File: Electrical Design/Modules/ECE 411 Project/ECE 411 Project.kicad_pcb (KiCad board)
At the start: 2 copper layers, 87.8 x 99.9 mm, 141 parts, among them J1 5mm 9V Barrel, J2 BOOST, J3 Pheonix Connector, J4 1/8in Jack, J5 1x2 header, J6 1x2header, J7 1x2header, M4 MountingHole_4.3mm_M4_Pad_Top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, Q2 2N3904, Q3 2N3904, Q4 2N3904, Q5 PNP, Q6 PNP, SW1 SW_Push, SW10 SW_SPDT, SW2 SW_Push, SW3 SW_Push, SW4 SW_Push, SW5 SW_Push, SW6 SW_Push, SW7 SW_Push, SW9 SW_SPDT, U1 HT7333, U2 LT1054, U3 MN3207, U4 NE555D, U5 LTV-827, U9 TPA3136D2PWPR

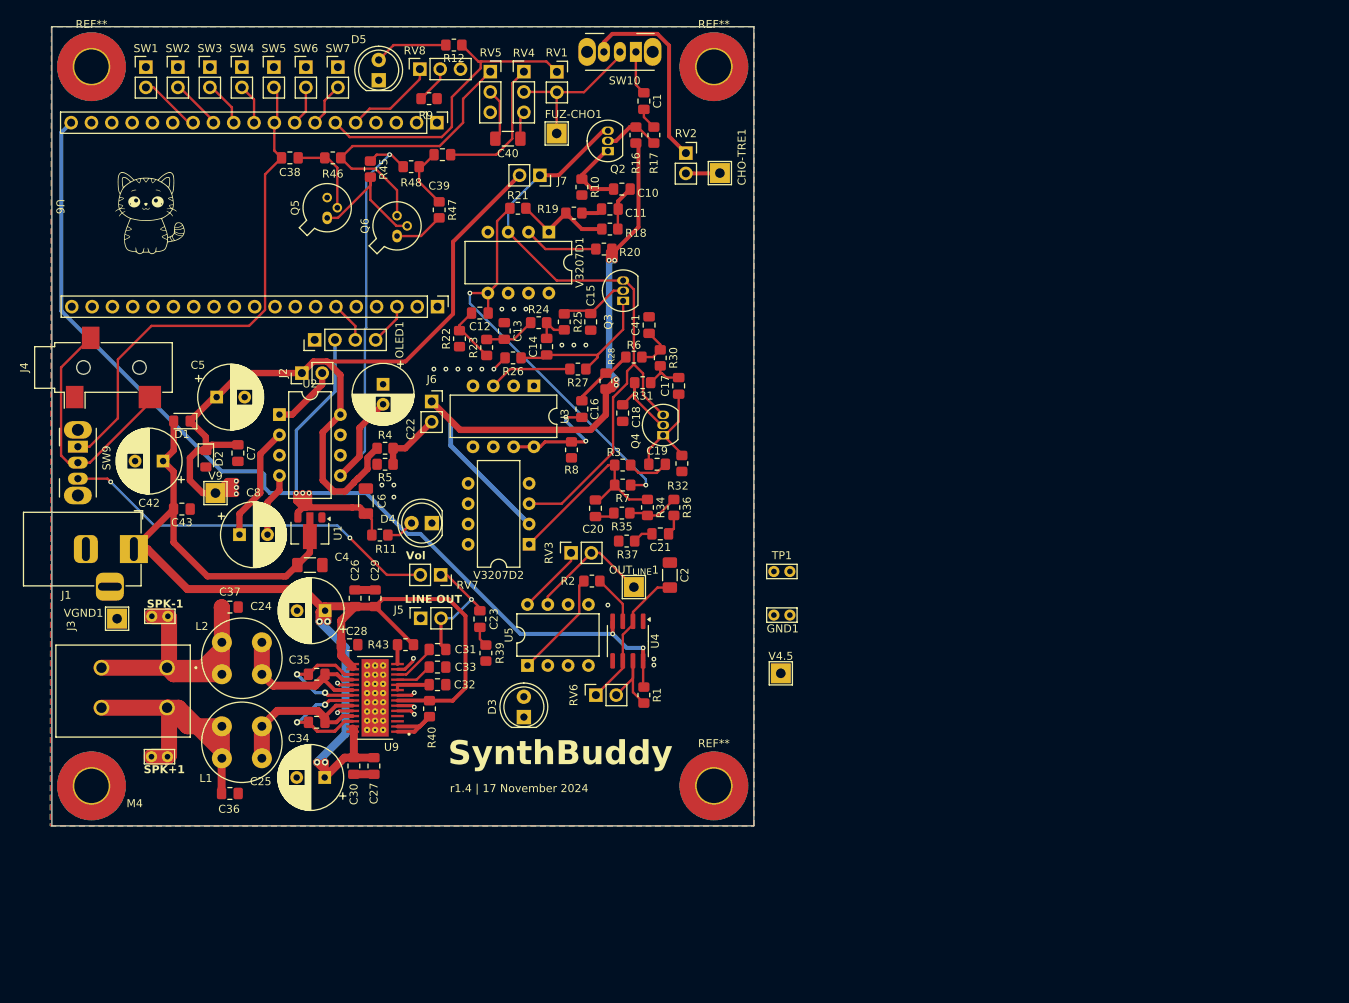
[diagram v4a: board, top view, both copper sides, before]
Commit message: add testpoints
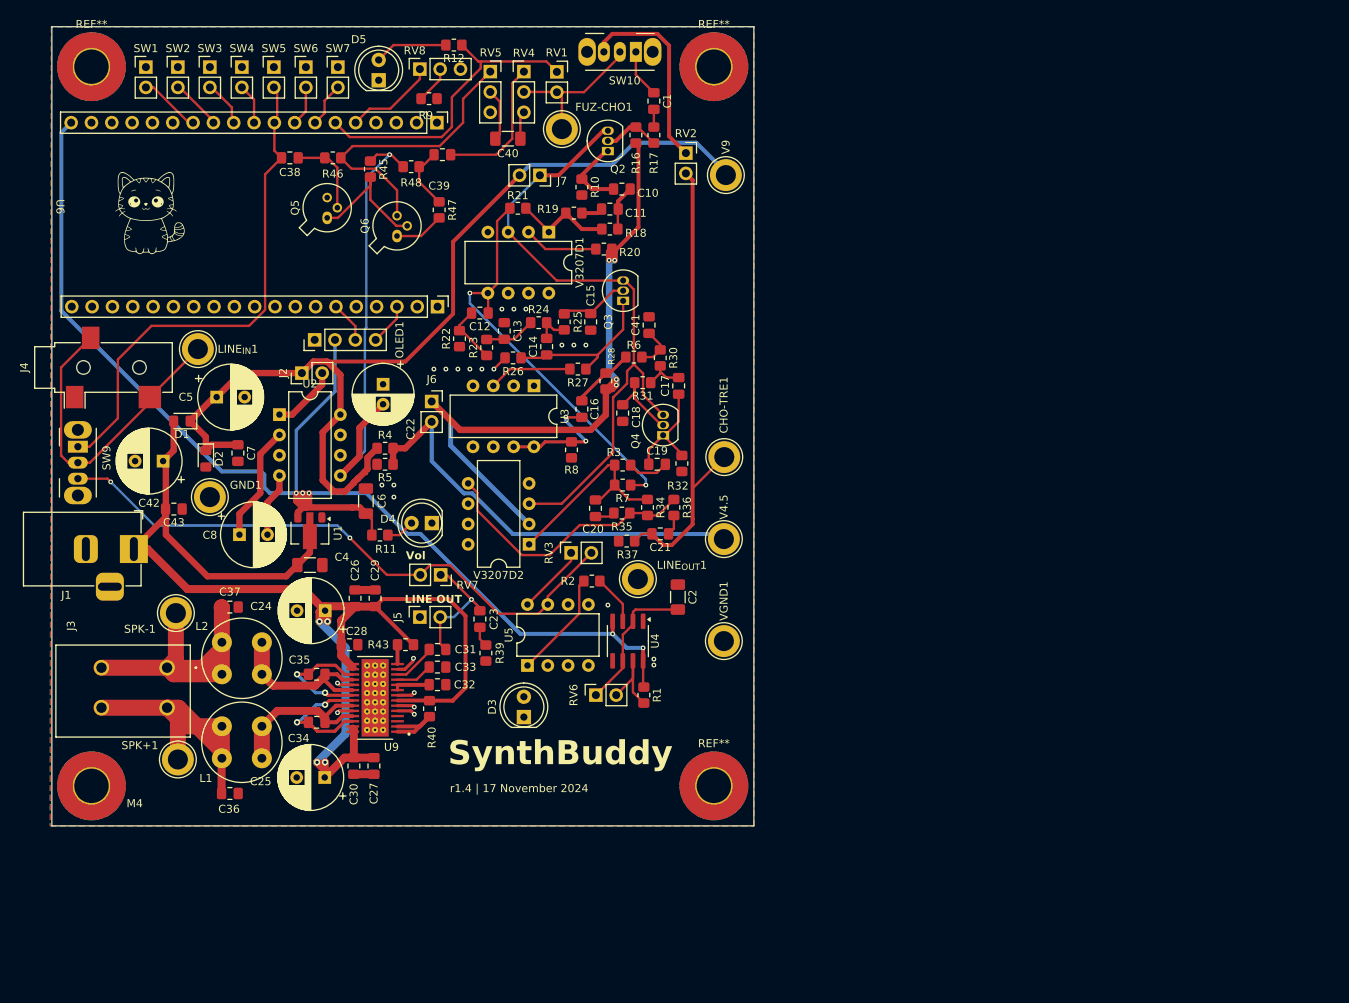
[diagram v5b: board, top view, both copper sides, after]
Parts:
- removed OUT_{LINE}1: TestPoint, TestPoint:TestPoint_THTPad_2.5x2.5mm_Drill1.2mm
- removed TP1: Line In, TestPoint:TestPoint_Bridge_Pitch2.0mm_Drill0.7mm
- added LINE_{IN}1: Line In, TestPoint:TestPoint_Loop_D3.80mm_Drill2.5mm, F.Cu at (50.0, 64.0)
- added LINE_{OUT}1: TestPoint, TestPoint:TestPoint_Loop_D3.80mm_Drill2.5mm, F.Cu at (105.0, 92.8)
- CHO-TRE1, FUZ-CHO1, V4.5, V9, VGND1: footprint TestPoint:TestPoint_THTPad_2.5x2.5mm_Drill1.2mm -> TestPoint:TestPoint_Loop_D3.80mm_Drill2.5mm
- GND1, SPK+1, SPK-1: footprint TestPoint:TestPoint_Bridge_Pitch2.0mm_Drill0.7mm -> TestPoint:TestPoint_Loop_D3.80mm_Drill2.5mm
- moved VGND1 75.9 mm to (115.8, 100.5)
- moved V9 75.2 mm to (116.0, 42.2), turned to 90 degrees
- moved GND1 72.0 mm to (51.5, 82.5)
- moved CHO-TRE1 35.5 mm to (115.8, 77.5)
- moved V4.5 18.2 mm to (115.8, 87.8), turned to 90 degrees
- moved SPK+1 3.32 mm to (47.5, 115.3)
- moved SPK-1 3.03 mm to (47.2, 97.0)
- moved C2 2.93 mm to (110.0, 95.0)
- moved C1 1.25 mm to (107.0, 33.0)
- moved C43 1.00 mm to (47.0, 84.0)
- moved FUZ-CHO1 0.85 mm to (95.5, 36.5)
- moved J5 0.18 mm to (77.8, 97.5)
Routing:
- net /Chorus Effect/CHORUSOUT: track 15.5 -> 71.6 mm
- net +4.5V: track 8.20 -> 53.7 mm
- net Net-(R34-Pad2): track 6.45 -> 33.9 mm
- net /Amp: track 63.6 -> 75.9 mm
- net +9V: track 112.7 -> 124.6 mm, vias 3 -> 0
- net /LineIn: track 31.5 -> 40.0 mm
- net /Class-D Amplification/SPK-: track 41.1 -> 39.7 mm
- net /Class-D Amplification/SPK+: track 42.7 -> 41.5 mm
- net /Chorus Effect/CHORUSIN: track 5.53 -> 6.04 mm
- net Net-(C1-Pad2): track 2.73 -> 2.21 mm

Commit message: update diode footptint, rounding edge cuts, some stitching
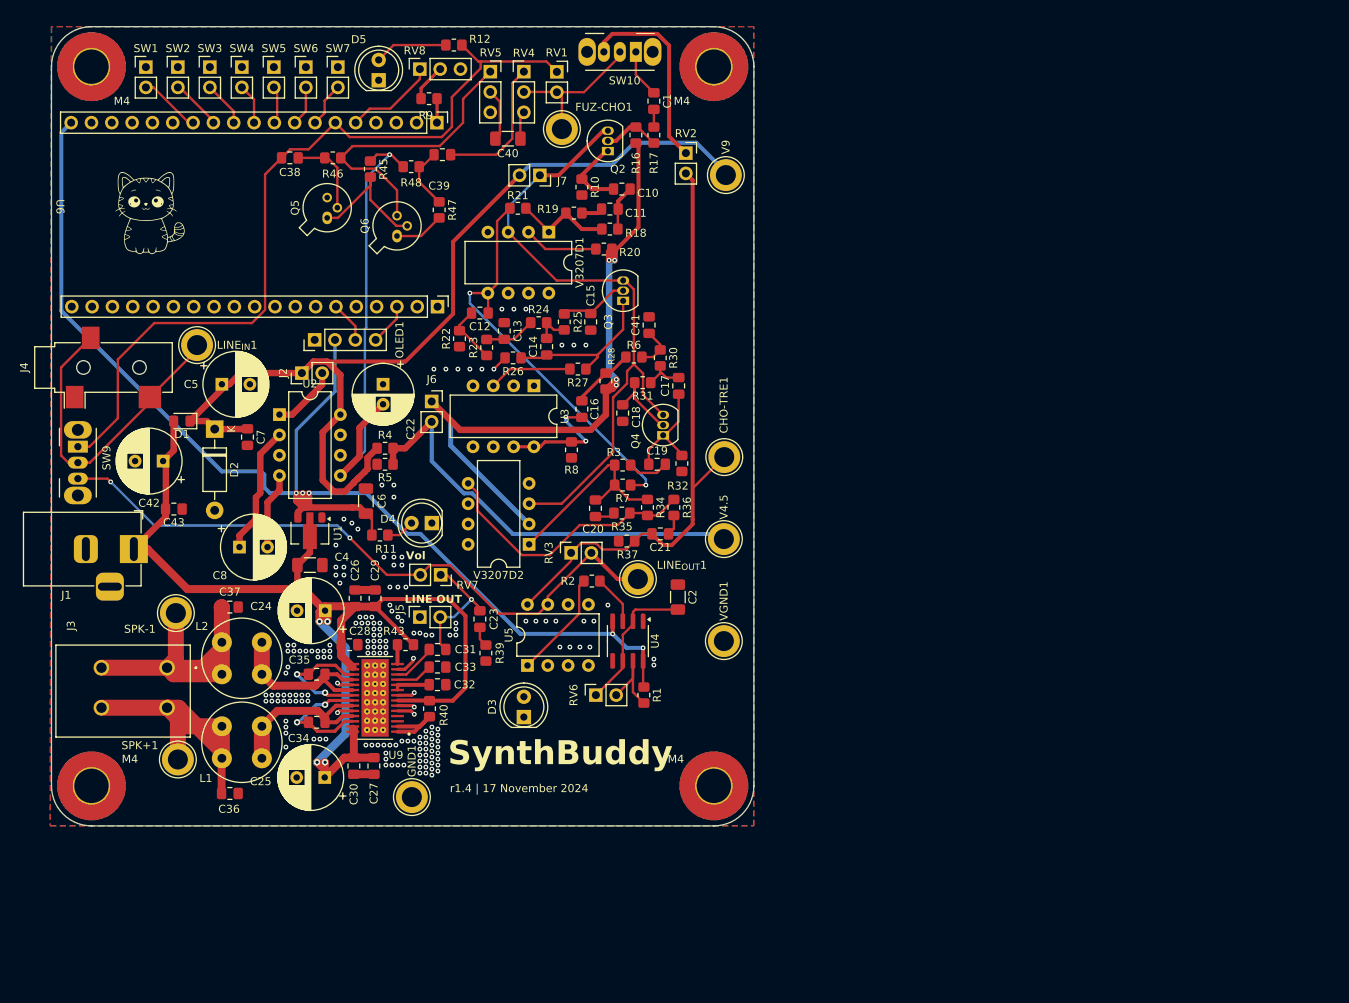
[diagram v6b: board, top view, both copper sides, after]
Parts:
- D2: footprint Diode_SMD:D_0805_2012Metric_Pad1.15x1.40mm_HandSolder -> Diode_THT:D_DO-41_SOD81_P10.16mm_Horizontal
- moved GND1 45.2 mm to (76.8, 120.0)
- moved D2 3.87 mm to (52.1, 74.0)
- moved C7 2.33 mm to (56.2, 75.0)
- moved C5 1.73 mm to (53.0, 68.4)
- moved C8 1.55 mm to (55.2, 88.8)
- moved LINE_{IN}1 0.51 mm to (49.9, 63.5)
- renumbered REF** to M4
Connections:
- SW3 pad 2: /ESP32-S3-WROOM Dev Board/BTN1 -> /ESP32-S3-WROOM Dev Board/BTN2
- U6 pad 11: /ESP32-S3-WROOM Dev Board/BTN1 -> /ESP32-S3-WROOM Dev Board/BTN2
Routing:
- net Vin: track 169.3 -> 150.3 mm
- net /Chorus Effect/CHORUSOUT: track 71.6 -> 80.8 mm
- net /Amp: track 75.9 -> 83.1 mm
- net /ESP32-S3-WROOM Dev Board/BTN1: track 12.2 -> 6.40 mm
- net /ESP32-S3-WROOM Dev Board/BTN2: track 0.00 -> 5.64 mm
- net /FX: track 98.2 -> 102.0 mm
- net /ESP32-S3-WROOM Dev Board/MCU3v3: track 0.00 -> 3.01 mm
- net Net-(U2-CAP+): track 14.5 -> 16.1 mm
- net Net-(U2-CAP-): track 8.01 -> 9.56 mm
- net +9V: track 124.6 -> 123.4 mm
- net GND: vias 24 -> 173
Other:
- outline, holes or cut-outs redrawn

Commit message: pcb finalization
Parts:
- moved C42 2.09 mm to (47.7, 78.4)
- moved C40 1.00 mm to (88.8, 38.7)
- moved RV4 0.98 mm to (90.8, 30.3)
- moved RV5 0.98 mm to (86.5, 30.3)
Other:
- board text added: "9V"
- board text added: "AMP: 20W MAX INTO 8Ω"
- board text added: "AUX IN"
- board text added: "AUX TO FX/AMP SELECT"
- board text added: "BOOST"
- board text added: "CHORUS BYPASS"
- board text added: "Center-Positive"
- board text added: "ESP32-WROOM-NARROW DEV BOARD"
- board text added: "board r1.5 | sch r2.5 | 18 November 2024"
- board text removed: "r1.4 | 17 November 2024"

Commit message: pcb madness
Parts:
- moved G*** 2.50 mm to (46.0, 45.5)
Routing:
- net Net-(D3-A): track 0.00 -> 5.15 mm
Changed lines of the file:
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@@
 	(footprint "LOGO"
 		(layer "F.Cu")
-		(at 44 47)
+		(at 46 45.5)
 		(property "Reference" "G***"
 			(at 0 0 0)
@@
 	)
 	(segment
+		(start 90.75 107.46)
+		(end 93.74 104.47)
+		(width 0.3)
+		(layer "F.Cu")
+		(net 96)
+	)
+	(segment
+		(start 93.74 104.47)
+		(end 93.74 103.55)
+		(width 0.3)
+		(layer "F.Cu")
+		(net 96)
+	)
+	(segment
